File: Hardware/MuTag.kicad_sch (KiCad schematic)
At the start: 29 parts, among them IC1 ST25DV04K-IER6S3, J1 Conn_01x02, J2 Conn_01x04, J3 Conn_01x06, U1 STM8L101F3P

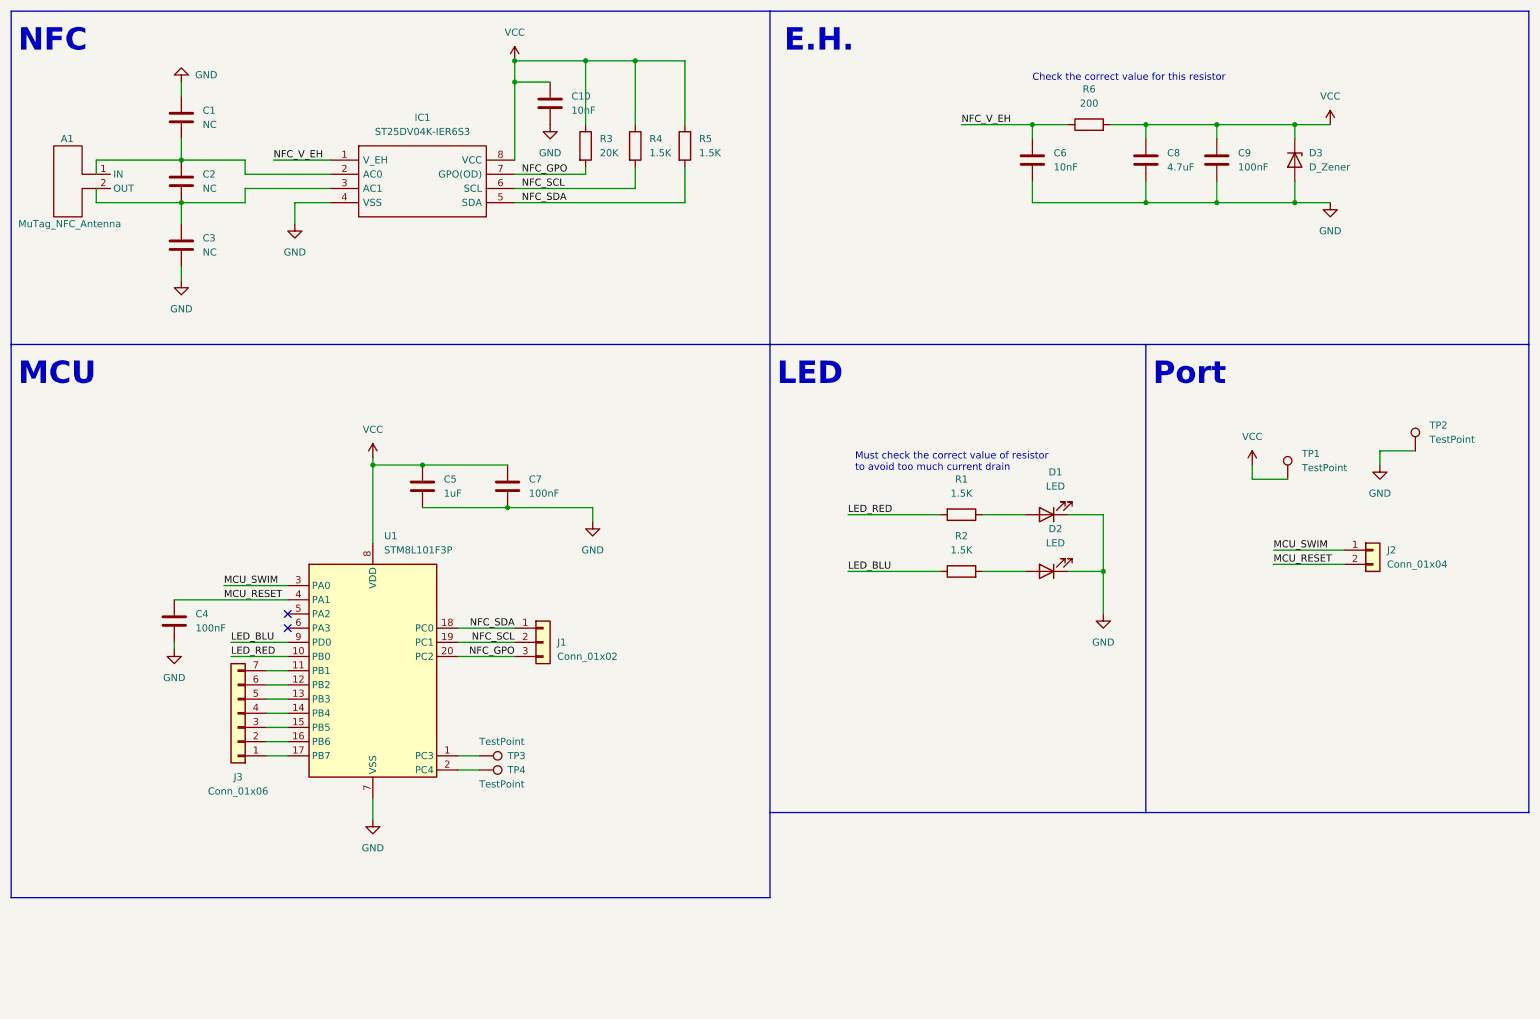
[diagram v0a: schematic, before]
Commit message: First routing of new version - no antenna
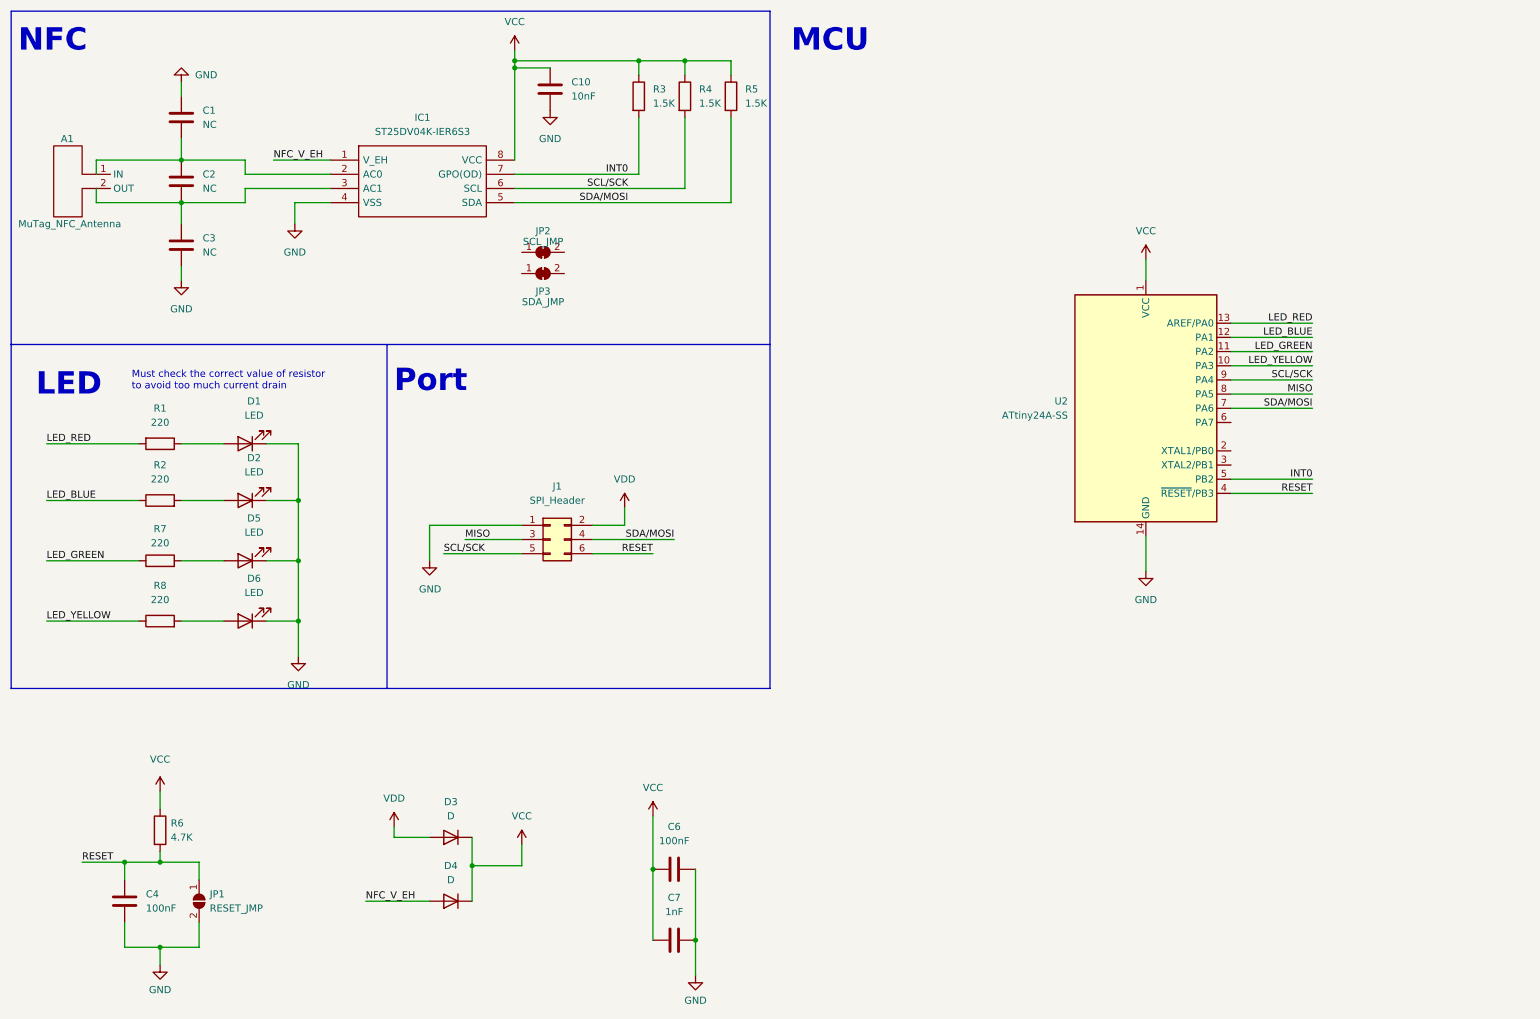
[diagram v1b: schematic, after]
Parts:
- removed C5: 1uF, Capacitor_SMD:C_0402_1005Metric, symbol Device:C
- removed C8: 4.7uF, Capacitor_SMD:C_0402_1005Metric, symbol Device:C
- removed C9: 100nF, Capacitor_SMD:C_0402_1005Metric, symbol Device:C
- removed D3: D_Zener, Diode_SMD:D_SOD-123, symbol Device:D_Zener
- removed J1: Conn_01x02, Connector_PinSocket_1.27mm:PinSocket_1x03_P1.27mm_Vertical_SMD_Pin1Right, symbol Connector_Generic:Conn_01x03
- removed J2: Conn_01x04, Connector_PinHeader_1.27mm:PinHeader_1x02_P1.27mm_Vertical_SMD_Pin1Right, symbol Connector_Generic:Conn_01x02
- removed J3: Conn_01x06, Connector_PinSocket_1.27mm:PinSocket_1x07_P1.27mm_Vertical_SMD_Pin1Right, symbol Connector_Generic:Conn_01x07
- removed TP1, TP2: TestPoint, TestPoint:TestPoint_Pad_1.5x1.5mm, symbol Connector:TestPoint
- removed TP3, TP4: TestPoint, TestPoint:TestPoint_Pad_D1.0mm, symbol Connector:TestPoint
- removed U1: STM8L101F3P, Package_SO:TSSOP-20_4.4x6.5mm_P0.65mm, symbol MCU_ST_STM8:STM8L101F3P
- added D3, D4: D, Diode_SMD:D_0402_1005Metric, symbol Device:D
- added D5, D6: LED, LED_SMD:LED_0603_1608Metric, symbol Device:LED
- added J1: SPI_Header, Connector_PinHeader_1.27mm:PinHeader_2x03_P1.27mm_Vertical, symbol Connector_Generic:Conn_02x03_Odd_Even
- added JP1: RESET_JMP, Jumper:SolderJumper-2_P1.3mm_Open_RoundedPad1.0x1.5mm, symbol Jumper:SolderJumper_2_Open
- added JP2: SCL_JMP, Jumper:SolderJumper-2_P1.3mm_Bridged_RoundedPad1.0x1.5mm, symbol Jumper:SolderJumper_2_Bridged
- added JP3: SDA_JMP, Jumper:SolderJumper-2_P1.3mm_Bridged_RoundedPad1.0x1.5mm, symbol Jumper:SolderJumper_2_Bridged
- added R7, R8: 220, Resistor_SMD:R_0402_1005Metric, symbol Device:R
- added U2: ATtiny24A-SS, Package_SO:SOIC-14_3.9x8.7mm_P1.27mm, symbol MCU_Microchip_ATtiny:ATtiny24A-SS
- C6: value 10nF -> 100nF
- C7: value 100nF -> 1nF
- R1, R2: value 1.5K -> 220
- R3: value 20K -> 1.5K
- R6: value 200 -> 4.7K
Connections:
- net GND: now also D5.1 (K), D6.1 (K), J1.1 (Pin_1), JP1.2 (B), U2.14 (GND)
- net LED_RED: now also U2.13 (AREF/PA0)
- net NFC_V_EH: now also D4.2 (A); no longer C6.1, R6.1
- net VCC: now also C6.1, R6.1, D3.1 (K), D4.1 (K), U2.1 (VCC); no longer R6.2
- net LED_BLU renamed LED_BLUE
- net LED_BLUE: now also U2.12 (PA1)
- net MCU_RESET renamed RESET
- net RESET: now also R6.2, J1.6 (Pin_6), JP1.1 (A), U2.4 (~{RESET}/PB3)
- net NFC_GPO renamed INT0
- net INT0: now also U2.5 (PB2)
- net NFC_SCL renamed SCL/SCK
- net SCL/SCK: now also J1.5 (Pin_5), U2.9 (PA4)
- net NFC_SDA renamed SDA/MOSI
- net SDA/MOSI: now also J1.4 (Pin_4), U2.7 (PA6)
- new net: D5.2 (A), R7.2
- new net: D6.2 (A), R8.2
- new net LED_GREEN: R7.1, U2.11 (PA2)
- new net LED_YELLOW: R8.1, U2.10 (PA3)
- new net MISO: J1.3 (Pin_3), U2.8 (PA5)
- new net VDD: D3.2 (A), J1.2 (Pin_2)
- no-connect marks 2 -> 0
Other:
- note removed: "Check the correct value for this resistor"
- note removed: "E.H."
- moved on the sheet: C10, D1, D2, R1, R2, R3, R4, R5

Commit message: New finished routing, with bigger antenna and leds - ready for production
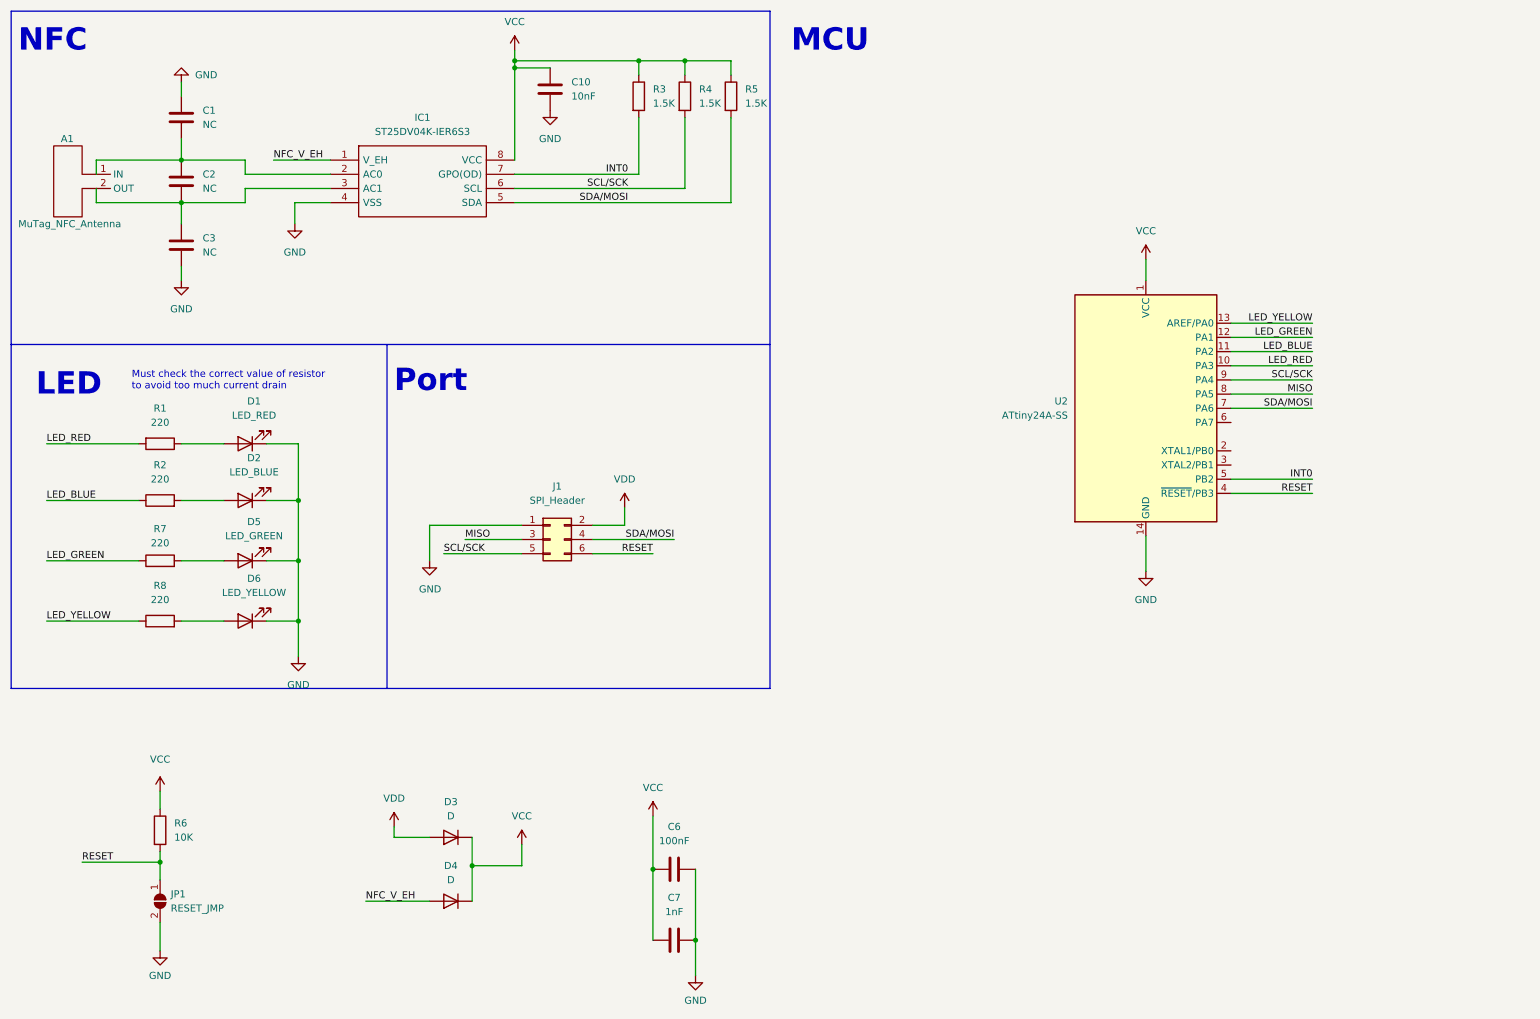
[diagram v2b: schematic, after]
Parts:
- removed C4: 100nF, Capacitor_SMD:C_0402_1005Metric, symbol Device:C
- removed JP2: SCL_JMP, Jumper:SolderJumper-2_P1.3mm_Bridged_RoundedPad1.0x1.5mm, symbol Jumper:SolderJumper_2_Bridged
- removed JP3: SDA_JMP, Jumper:SolderJumper-2_P1.3mm_Bridged_RoundedPad1.0x1.5mm, symbol Jumper:SolderJumper_2_Bridged
- A1: footprint MuTag Antenna:mutag_antenna -> MuTag Antenna:mutag_new_antenna
- D1: value LED -> LED_RED
- D2: value LED -> LED_BLUE
- D3, D4: footprint Diode_SMD:D_0402_1005Metric -> Diode_SMD:D_SOD-123F
- D5: value LED -> LED_GREEN
- D6: value LED -> LED_YELLOW
- R6: value 4.7K -> 10K
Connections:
- net LED_BLUE: now also U2.11 (PA2); no longer U2.12 (PA1)
- net LED_GREEN: now also U2.12 (PA1); no longer U2.11 (PA2)
- net LED_RED: now also U2.10 (PA3); no longer U2.13 (AREF/PA0)
- net LED_YELLOW: now also U2.13 (AREF/PA0); no longer U2.10 (PA3)
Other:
- moved on the sheet: JP1

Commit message: Second version first commit - produced and tested: all working
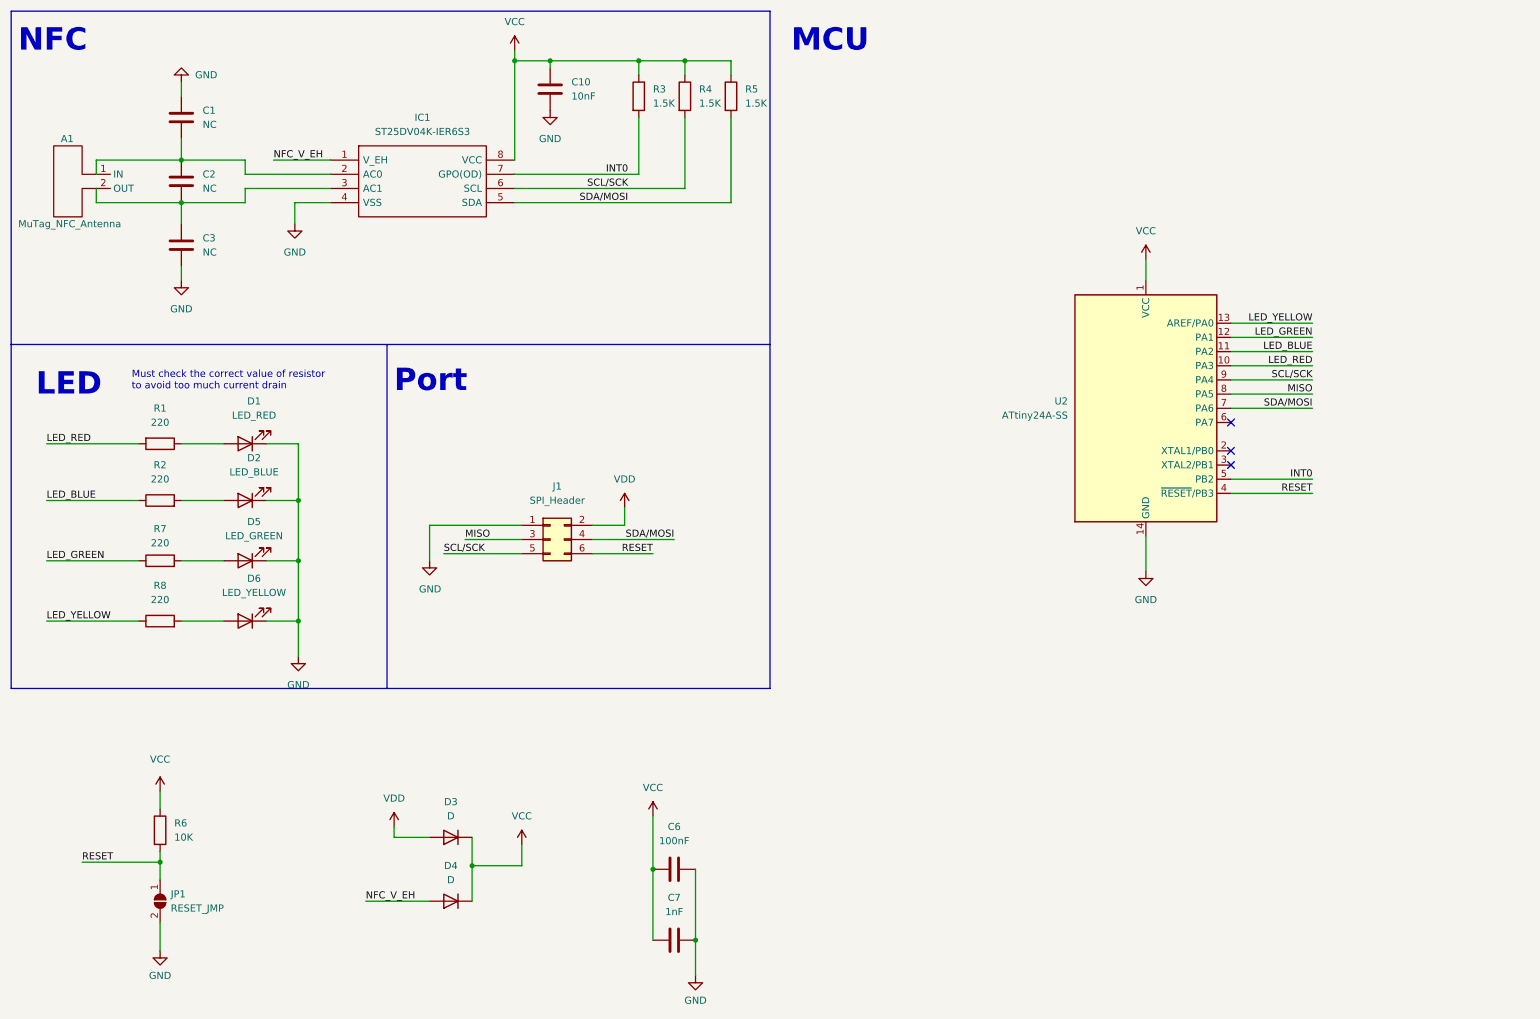
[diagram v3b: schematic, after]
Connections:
- no-connect marks 0 -> 3

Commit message: Version v2.1 - Set production and docs with ATTiny44a, removed diode from VCC port, moved components to fit bigger port, led resistors value changed to 160
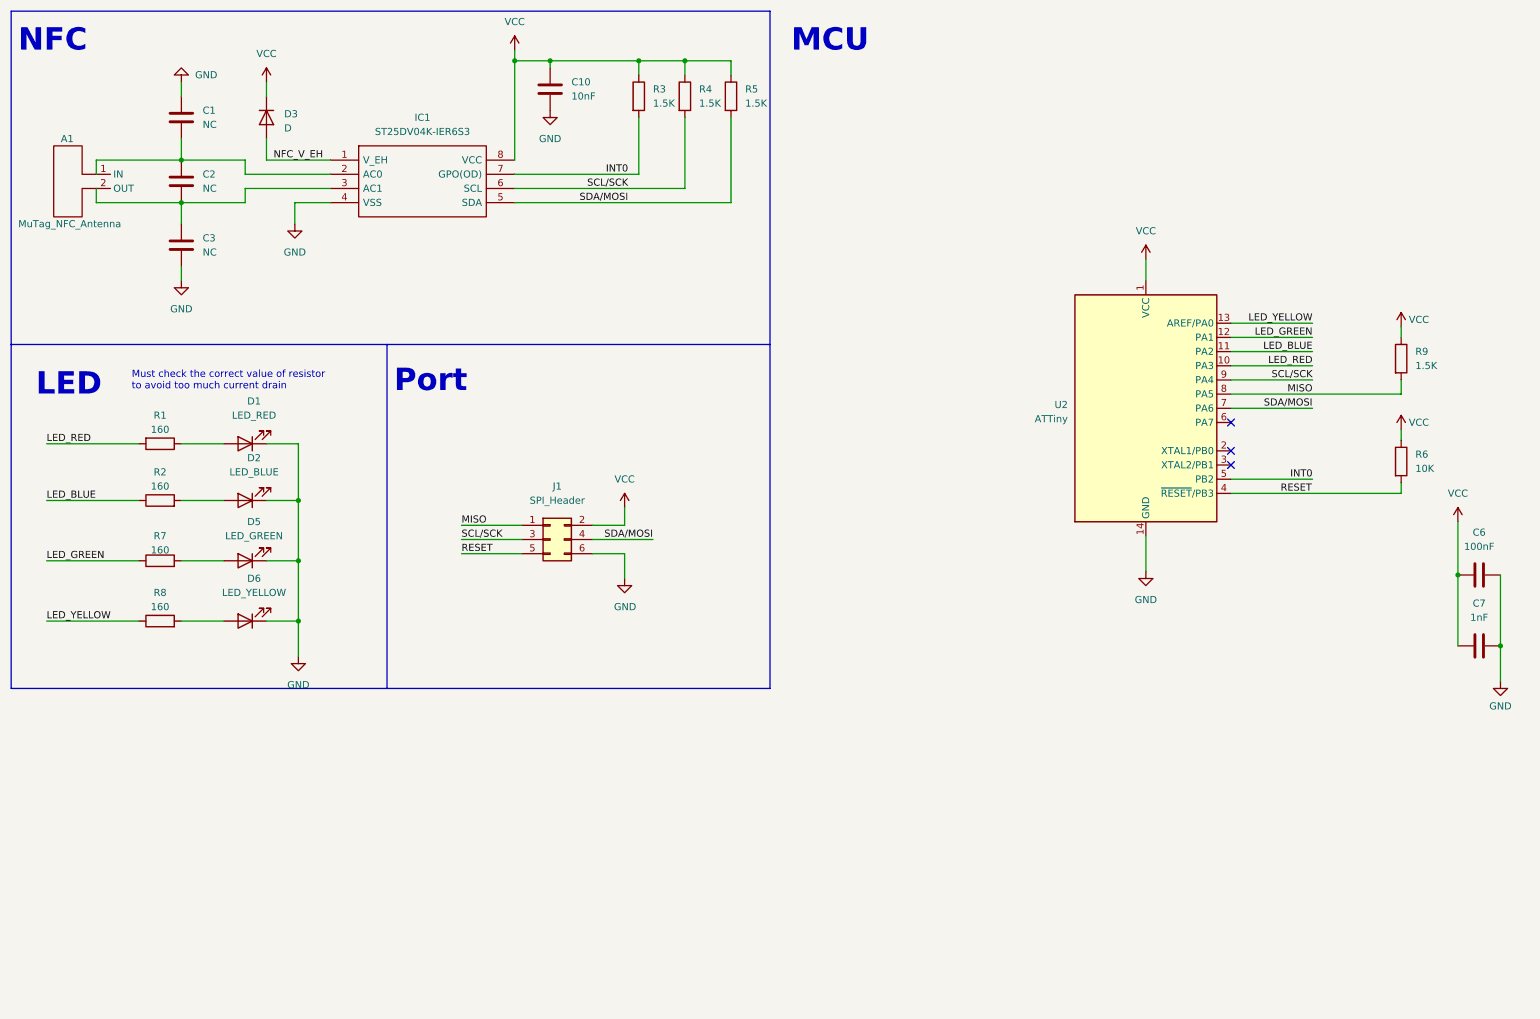
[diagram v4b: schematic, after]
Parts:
- removed D4: D, Diode_SMD:D_SOD-123F, symbol Device:D
- removed JP1: RESET_JMP, Jumper:SolderJumper-2_P1.3mm_Open_RoundedPad1.0x1.5mm, symbol Jumper:SolderJumper_2_Open
- added R9: 1.5K, Resistor_SMD:R_0402_1005Metric, symbol Device:R
- J1: footprint Connector_PinHeader_1.27mm:PinHeader_2x03_P1.27mm_Vertical -> Connector_PinHeader_2.54mm:PinHeader_2x03_P2.54mm_Vertical
- R1, R2, R7, R8: value 220 -> 160
- U2: value ATtiny24A-SS -> ATTiny
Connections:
- net GND: now also J1.6 (Pin_6); no longer J1.1 (Pin_1)
- net MISO: now also J1.1 (Pin_1), R9.2; no longer J1.3 (Pin_3)
- net NFC_V_EH: now also D3.2 (A)
- net RESET: now also J1.5 (Pin_5); no longer J1.6 (Pin_6)
- net SCL/SCK: now also J1.3 (Pin_3); no longer J1.5 (Pin_5)
- net VCC: now also J1.2 (Pin_2), R9.1
- removed net VDD: D3.2 (A), J1.2 (Pin_2)
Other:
- moved on the sheet: C6, C7, R6
